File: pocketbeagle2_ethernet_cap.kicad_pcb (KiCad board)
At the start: 4 copper layers, 35.3 x 55.3 mm, 78 parts, among them J1 RJ45_1840888-1, J2 Header_18x02_2.54mm_2.54mm_St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, J3 Header_18x02_2.54mm_2.54mm_St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, Q1 BSS138LT1G, Q2 BSS138LT1G, Q3 BSS138LT1G, U1 PocketBeagle2, U2 DP83867IRPAPR, U3 TPS7A2011PDBVR, U4 TPS7A2025PDBVR, Y1 25M

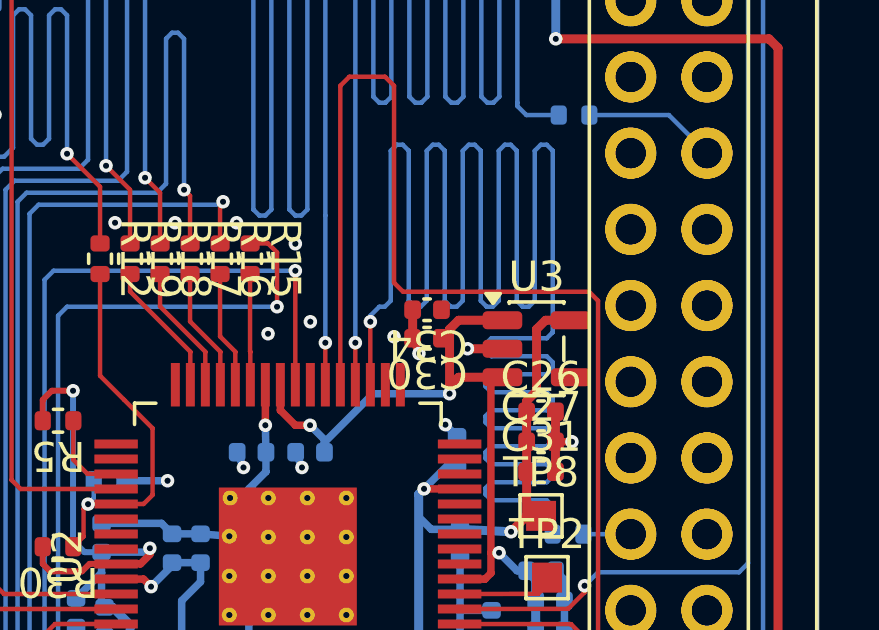
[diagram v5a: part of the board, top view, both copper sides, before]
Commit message: Add 3D models, fix PB2 stack height, C34 stub
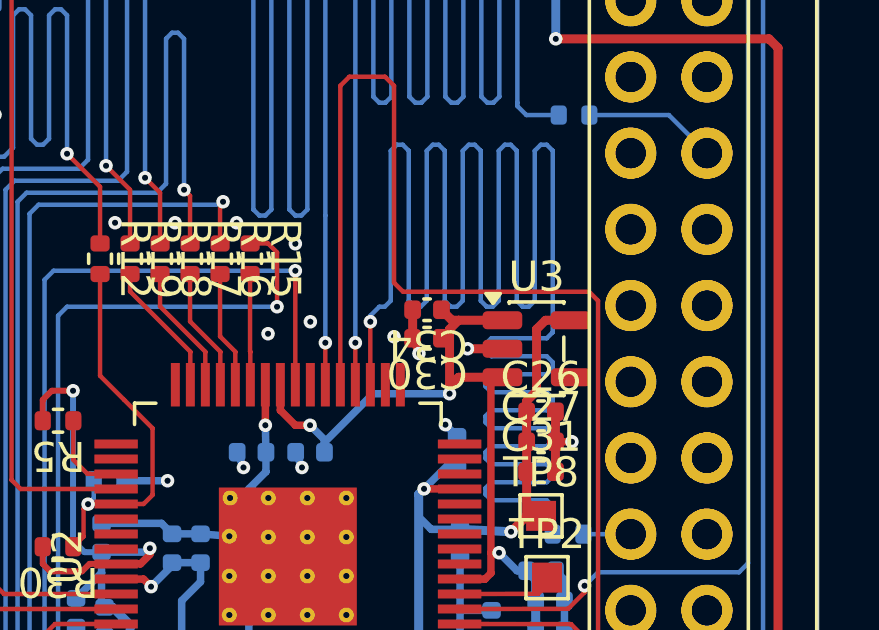
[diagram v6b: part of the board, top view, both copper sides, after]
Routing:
- net /VDD_3V3: track 176.1 -> 176.8 mm

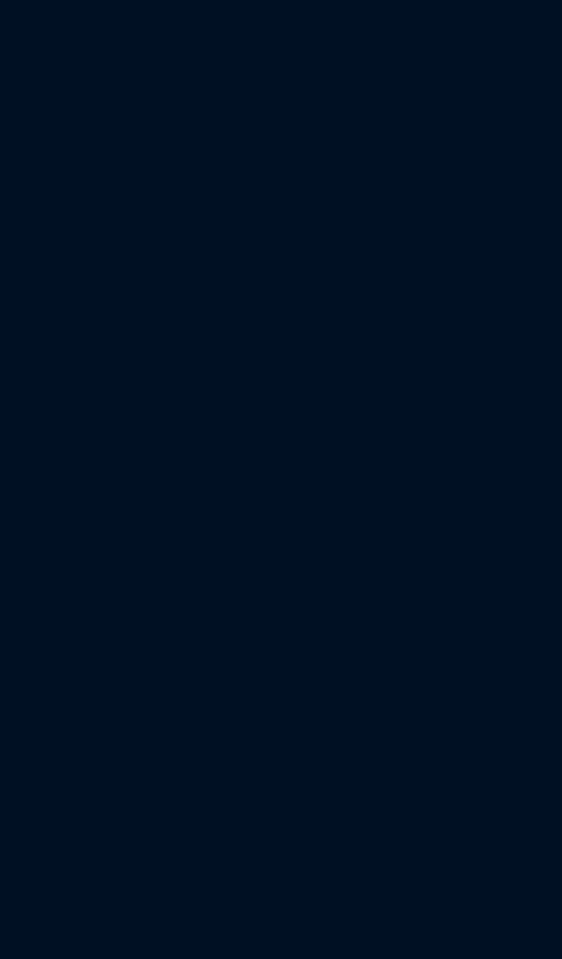
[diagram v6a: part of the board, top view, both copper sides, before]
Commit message: Add 1uF decoupling on PHY pins 4, 12, 41, 42
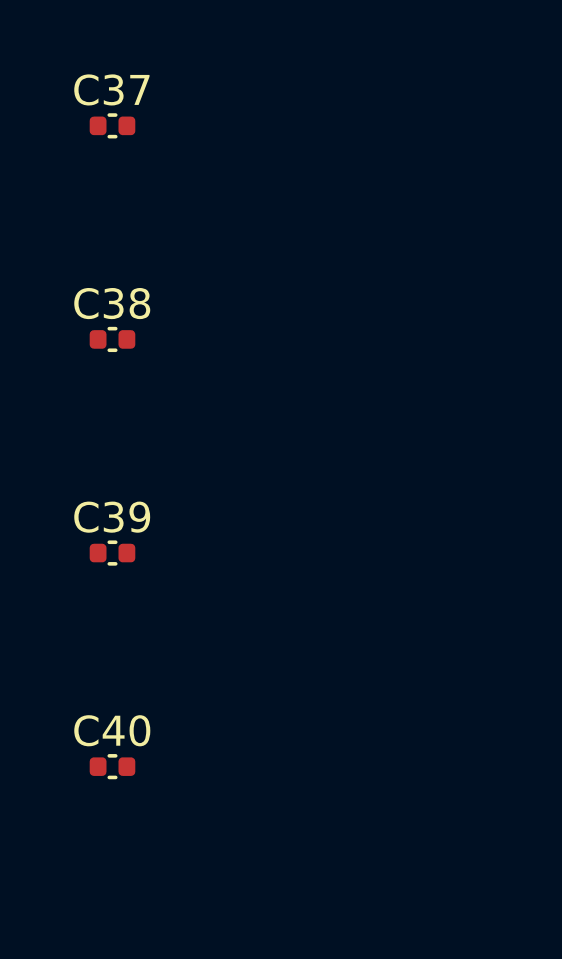
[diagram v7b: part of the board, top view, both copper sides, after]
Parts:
- added C37: 1u, KL_Footprints:C_0402, F.Cu at (5.91, 1.06)
- added C38: 1u, KL_Footprints:C_0402, F.Cu at (5.91, 8.18)
- added C39: 1u, KL_Footprints:C_0402, F.Cu at (5.91, 15.3)
- added C40: 1u, KL_Footprints:C_0402, F.Cu at (5.91, 22.4)

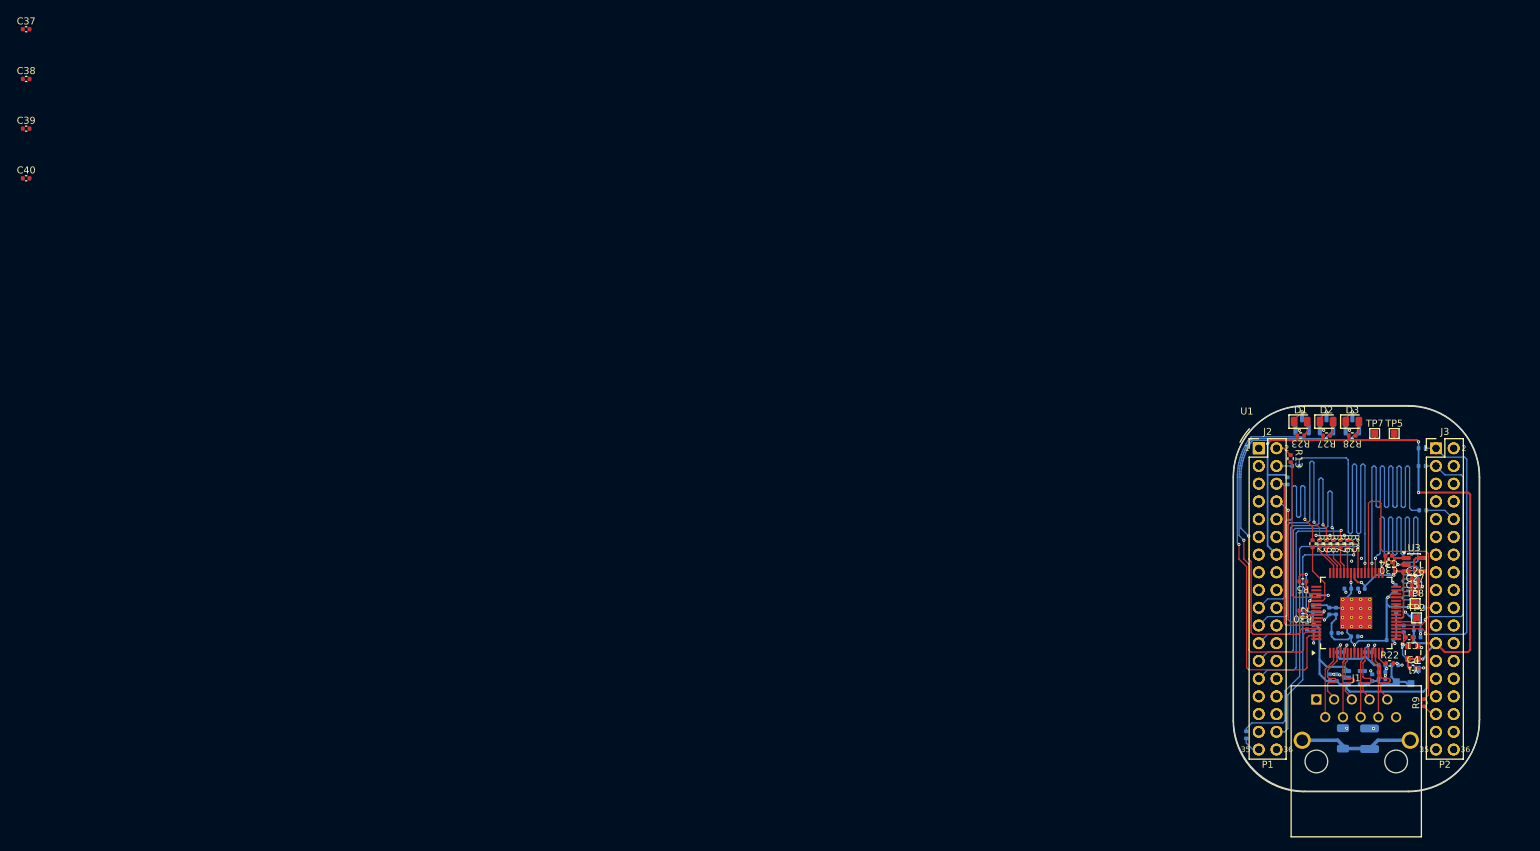
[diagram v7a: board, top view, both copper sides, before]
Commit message: Move J1 to bottom, rebuild MDI, U4 area, chassis planes
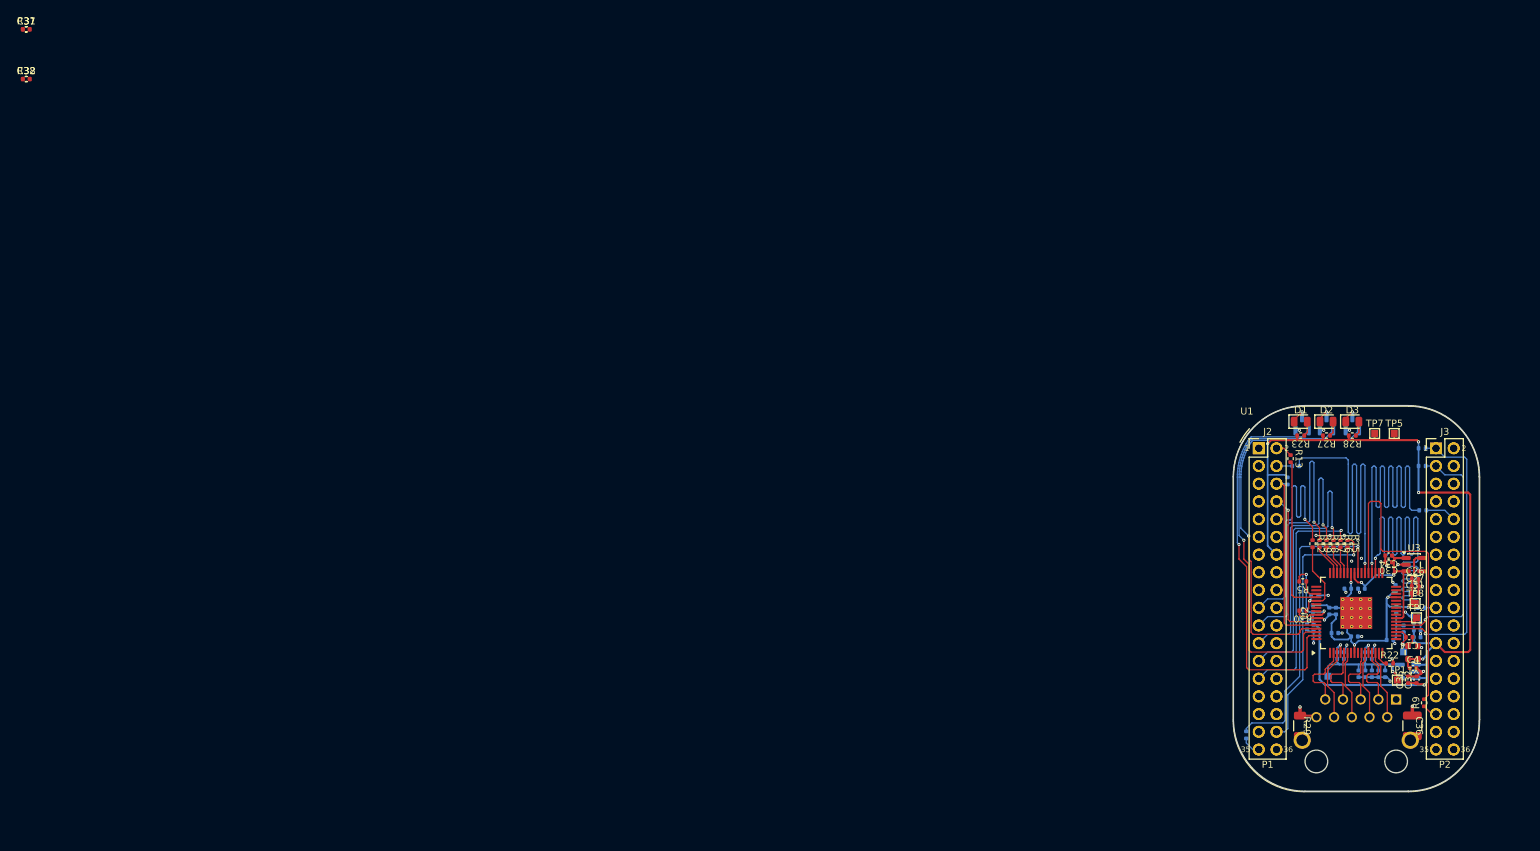
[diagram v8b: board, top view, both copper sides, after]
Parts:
- added R31: 5K76, KL_Footprints:R_0402, F.Cu at (5.93, 1.07)
- added R32: 2K49, KL_Footprints:R_0402, F.Cu at (5.93, 8.21)
- C32, C35, C36, R29, TP1: moved to F.Cu
- C39, C40, J1: moved to B.Cu
- moved C40 204.4 mm to (198.3, 91.3)
- moved C39 203.2 mm to (194.3, 91.3)
- moved C32 12.4 mm to (205.2, 94.3)
- moved TP6 11.9 mm to (192.5, 93.8)
- moved C35 10.3 mm to (204.0, 94.3)
- moved U4 7.75 mm to (204.0, 93.1), turned to 180 degrees
- moved R29 6.42 mm to (188.5, 100.9)
- moved C36 6.40 mm to (204.6, 100.9)
- moved C11 3.58 mm to (196.9, 93.5), turned to -90 degrees
- moved TP4 3.17 mm to (203.3, 90.3)
- moved C15 2.66 mm to (199.8, 93.5), turned to -90 degrees
- moved C8 2.41 mm to (197.8, 93.5), turned to -90 degrees
- moved C33 1.93 mm to (200.7, 93.5), turned to -90 degrees
- moved C19 1.63 mm to (198.8, 93.5), turned to -90 degrees
- moved TP1 0.29 mm to (202.4, 94.3)
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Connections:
- J1 pad 2: /network/phy/MDI0_PHY_RJ45_P -> /network/phy/MDI3_PHY_RJ45_N
- J1 pad 3: /network/phy/MDI0_PHY_RJ45_N -> /network/phy/MDI3_PHY_RJ45_P
- J1 pad 4: /network/phy/MDI1_PHY_RJ45_P -> /network/phy/MDI2_PHY_RJ45_N
- J1 pad 5: /network/phy/MDI1_PHY_RJ45_N -> /network/phy/MDI2_PHY_RJ45_P
- J1 pad 6: /network/phy/MDI2_PHY_RJ45_P -> /network/phy/MDI1_PHY_RJ45_N
- J1 pad 7: /network/phy/MDI2_PHY_RJ45_N -> /network/phy/MDI1_PHY_RJ45_P
- J1 pad 8: /network/phy/MDI3_PHY_RJ45_P -> /network/phy/MDI0_PHY_RJ45_N
- J1 pad 9: /network/phy/MDI3_PHY_RJ45_N -> /network/phy/MDI0_PHY_RJ45_P
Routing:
- net /network/rj45_connector_port0/CHASSIS: track 16.7 -> 1.35 mm
- net GND: track 39.0 -> 46.7 mm, vias 35 -> 30
- net /VDD_2V5: track 25.0 -> 28.4 mm, vias 2 -> 3
- net /network/oscillator/CLK_25M_OSC_to_PHY: track 9.34 -> 6.03 mm
- net /VDD_3V3: track 176.8 -> 176.7 mm, vias 9 -> 10
